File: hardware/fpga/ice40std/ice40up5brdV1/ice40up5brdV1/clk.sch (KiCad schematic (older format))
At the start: 0 parts

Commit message: usb => mcu => ice40 fpga => NAND flash bridge started
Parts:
- added C?: 0.01uF, Capacitor_SMD:C_0402_1005Metric, symbol Device:C
- added X?: ASE-xxxMHz, Oscillator:Oscillator_SMD_Abracon_ASE-4Pin_3.2x2.5mm, symbol Oscillator:ASE-xxxMHz
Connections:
- new net +3V3: C?.1, X?.1 (EN), X?.4 (Vdd)
- new net GND: C?.2, X?.2 (GND)
- new net clk: X?.3 (OUT)
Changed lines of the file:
@@
 Comment4 ""
 $EndDescr
+$Comp
+L Oscillator:ASE-xxxMHz X?
+U 1 1 60AB6E27
+P 3650 3800
+F 0 "X?" H 3994 3846 50  0000 L CNN
+F 1 "ASE-xxxMHz" H 3994 3755 50  0000 L CNN
+F 2 "Oscillator:Oscillator_SMD_Abracon_ASE-4Pin_3.2x2.5mm" H 4350 3450 50  0001 C CNN
+F 3 "http://www.abracon.com/Oscillators/ASV.pdf" H 3550 3800 50  0001 C CNN
+	1    3650 3800
+	1    0    0    -1
+$EndComp
+$Comp
+L Device:C C?
+U 1 1 60AB7231
+P 5250 3800
+F 0 "C?" H 5365 3846 50  0000 L CNN
+F 1 "0.01uF" H 5365 3755 50  0000 L CNN
+F 2 "Capacitor_SMD:C_0402_1005Metric" H 5288 3650 50  0001 C CNN
+F 3 "~" H 5250 3800 50  0001 C CNN
+	1    5250 3800
+	1    0    0    -1
+$EndComp
+$Comp
+L power:GND #PWR?
+U 1 1 60AB7989
+P 4500 4600
+F 0 "#PWR?" H 4500 4350 50  0001 C CNN
+F 1 "GND" H 4505 4427 50  0000 C CNN
+F 2 "" H 4500 4600 50  0001 C CNN
+F 3 "" H 4500 4600 50  0001 C CNN
+	1    4500 4600
+	1    0    0    -1
+$EndComp
+Wire Wire Line
+	3650 4100 3650 4300
+Wire Wire Line
+	3650 4300 4500 4300
+Wire Wire Line
+	4500 4300 4500 4600
+Wire Wire Line
+	4500 4300 5250 4300
+Wire Wire Line
+	5250 4300 5250 3950
+Connection ~ 4500 4300
+$Comp
+L power:+3V3 #PWR?
+U 1 1 60AB7CF6
+P 4500 2900
+F 0 "#PWR?" H 4500 2750 50  0001 C CNN
+F 1 "+3V3" H 4515 3073 50  0000 C CNN
+F 2 "" H 4500 2900 50  0001 C CNN
+F 3 "" H 4500 2900 50  0001 C CNN
+	1    4500 2900
+	1    0    0    -1
+$EndComp
+Wire Wire Line
+	3650 3500 3650 3300
+Wire Wire Line
+	3650 3300 4500 3300
+Wire Wire Line
+	4500 3300 4500 2900
+Wire Wire Line
+	4500 3300 5250 3300
+Wire Wire Line
+	5250 3300 5250 3650
+Connection ~ 4500 3300
+Wire Wire Line
+	3350 3800 3100 3800
+Wire Wire Line
+	3100 3800 3100 3300
+Wire Wire Line
+	3100 3300 3650 3300
+Connection ~ 3650 3300
+Text GLabel 3950 3800 2    50   Input ~ 0
+clk
 $EndSCHEMATC

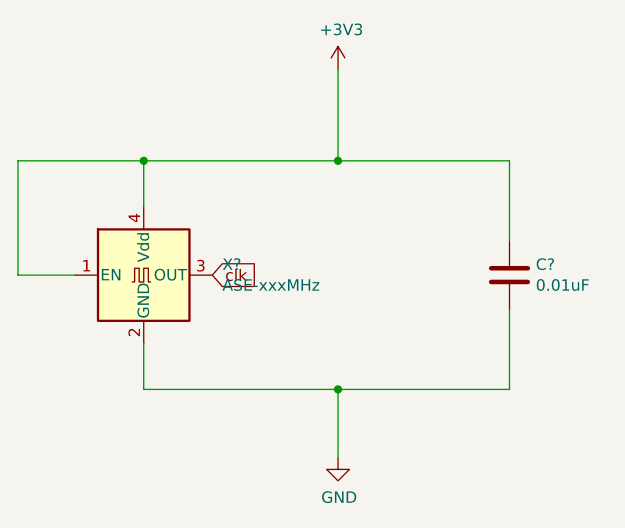
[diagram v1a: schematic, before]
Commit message: usb => mcu => ice40 fpga => NAND flash bridge started
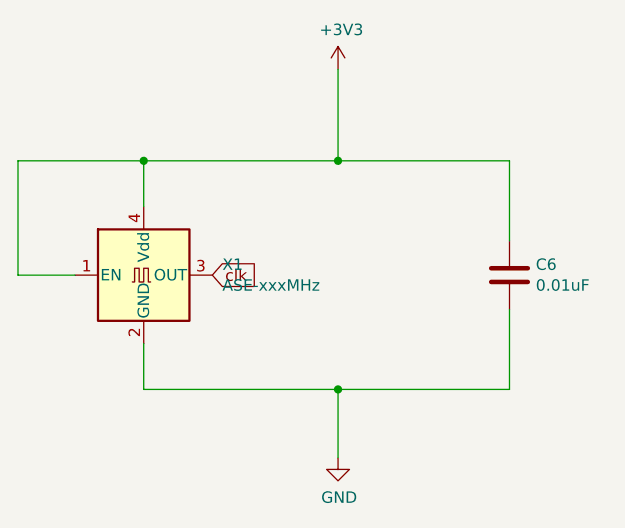
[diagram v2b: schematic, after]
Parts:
- gave numbers to parts that had none: 2
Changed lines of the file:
@@
 $EndDescr
 $Comp
-L Oscillator:ASE-xxxMHz X?
+L Oscillator:ASE-xxxMHz X1
 U 1 1 60AB6E27
 P 3650 3800
-F 0 "X?" H 3994 3846 50  0000 L CNN
+F 0 "X1" H 3994 3846 50  0000 L CNN
 F 1 "ASE-xxxMHz" H 3994 3755 50  0000 L CNN
 F 2 "Oscillator:Oscillator_SMD_Abracon_ASE-4Pin_3.2x2.5mm" H 4350 3450 50  0001 C CNN
@@
 $EndComp
 $Comp
-L Device:C C?
+L Device:C C6
 U 1 1 60AB7231
 P 5250 3800
-F 0 "C?" H 5365 3846 50  0000 L CNN
+F 0 "C6" H 5365 3846 50  0000 L CNN
 F 1 "0.01uF" H 5365 3755 50  0000 L CNN
 F 2 "Capacitor_SMD:C_0402_1005Metric" H 5288 3650 50  0001 C CNN
@@
 $EndComp
 $Comp
-L power:GND #PWR?
+L power:GND #PWR013
 U 1 1 60AB7989
 P 4500 4600
-F 0 "#PWR?" H 4500 4350 50  0001 C CNN
+F 0 "#PWR013" H 4500 4350 50  0001 C CNN
 F 1 "GND" H 4505 4427 50  0000 C CNN
 F 2 "" H 4500 4600 50  0001 C CNN
@@
 Connection ~ 4500 4300
 $Comp
-L power:+3V3 #PWR?
+L power:+3V3 #PWR012
 U 1 1 60AB7CF6
 P 4500 2900
-F 0 "#PWR?" H 4500 2750 50  0001 C CNN
+F 0 "#PWR012" H 4500 2750 50  0001 C CNN
 F 1 "+3V3" H 4515 3073 50  0000 C CNN
 F 2 "" H 4500 2900 50  0001 C CNN
